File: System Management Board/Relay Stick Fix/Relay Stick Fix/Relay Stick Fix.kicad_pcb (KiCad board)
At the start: 4 copper layers, 28.2 x 27 mm, 17 parts, among them J1 Conn_02x06, Q1 NMOS, U2 74LVC1G04

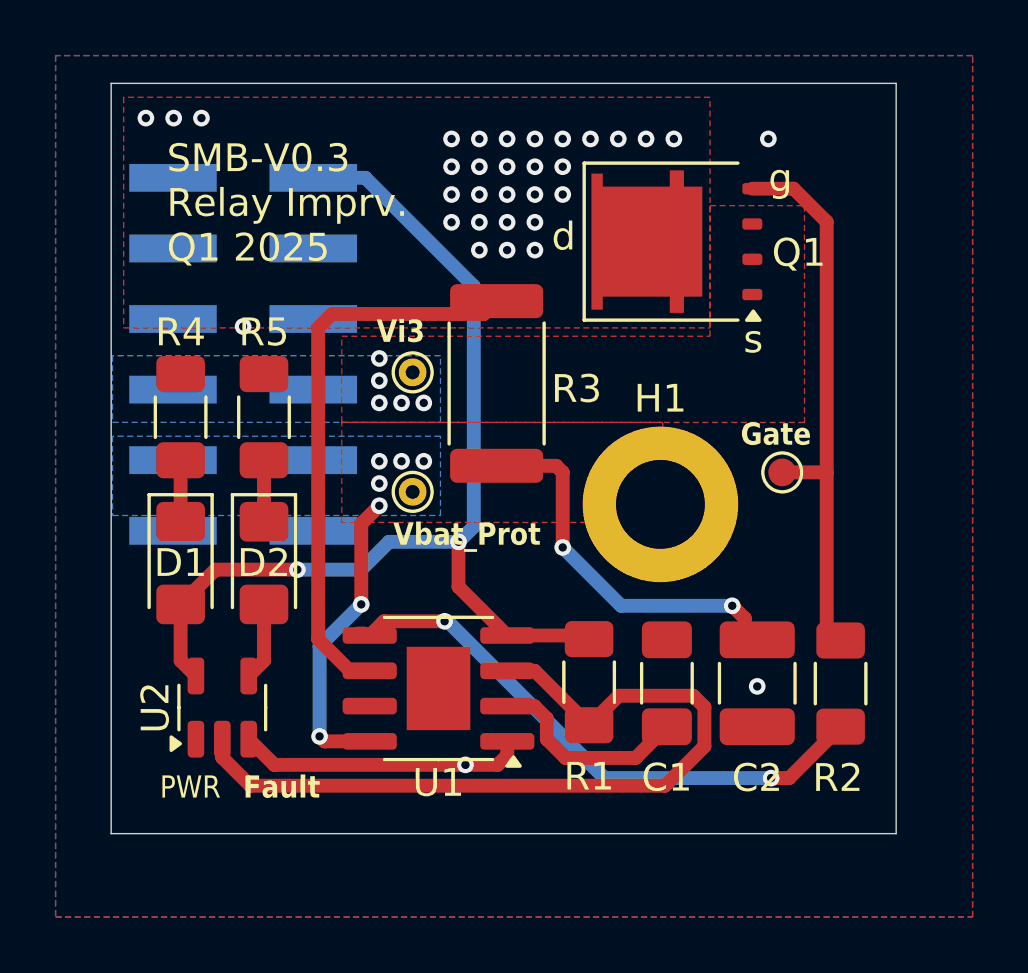
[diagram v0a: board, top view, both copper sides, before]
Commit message: fixed a mjor issue where 5V boot strap and GND headers were reversed
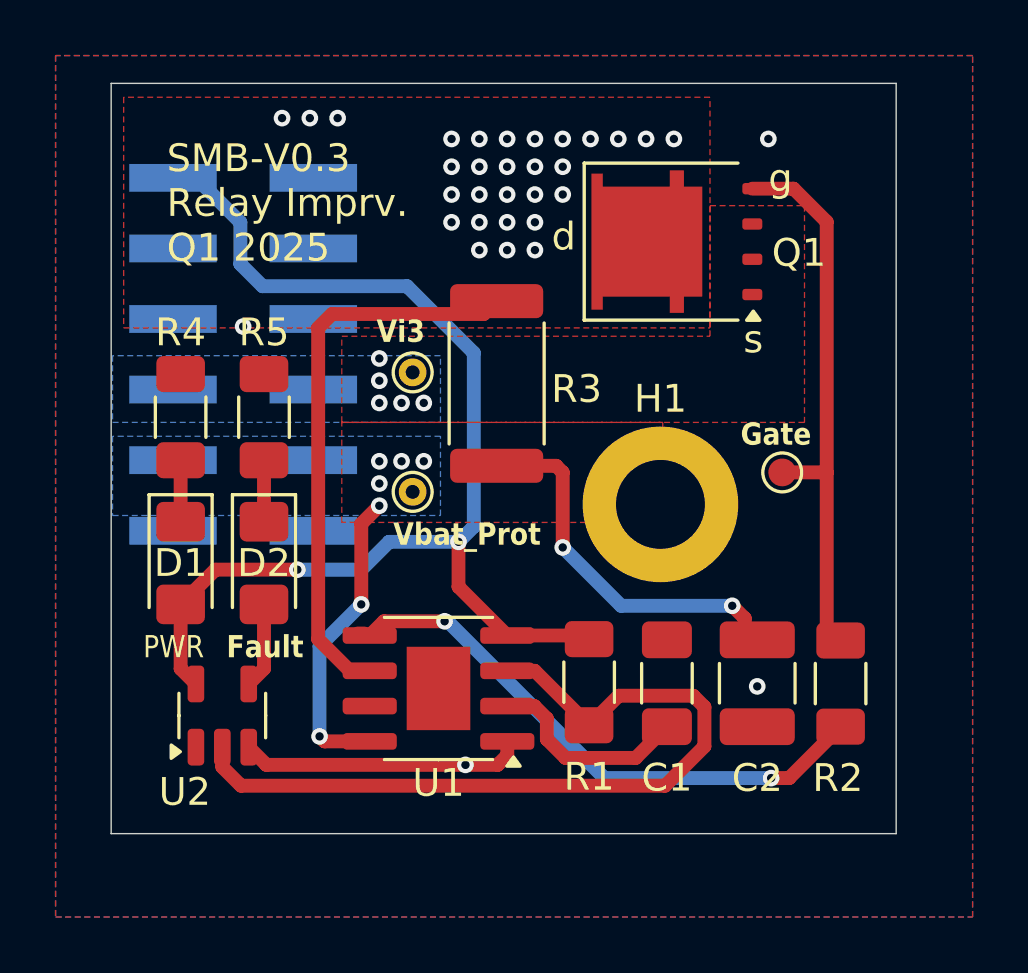
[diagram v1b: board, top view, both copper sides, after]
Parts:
- R3: value 0 -> .001
- moved U2 0.29 mm to (19.9, 37.8)
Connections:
- J1 pad 1: /5V Bootstrap -> GND
- J1 pad 2: GND -> /5V Bootstrap
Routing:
- net /5V Bootstrap: track 38.3 -> 42.8 mm
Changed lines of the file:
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@@
 	(footprint "Package_TO_SOT_SMD:SOT-23-5"
 		(layer "F.Cu")
-		(at 19.85 37.4625 90)
+		(at 19.85 37.75 90)
 		(descr "SOT, 5 Pin (https://www.jedec.org/sites/default/files/docs/Mo-178c.PDF variant AA), generated with kicad-footprint-generator ipc_gullwing_generator.py")
 		(tags "SOT TO_SOT_SMD")
 		(property "Reference" "U2"
-			(at 0 -2.4 -90)
+			(at -2.75 -1.35 0)
 			(layer "F.SilkS")
 			(effects
@@
 			)
 		)
-		(property "Value" "0"
+		(property "Value" ".001"
 			(at 0 2.62 -90)
 			(layer "F.Fab")
@@
 			(size 3.15 1)
 			(layers "B.Cu" "B.Paste" "B.Mask")
-			(net 2 "/5V Bootstrap")
+			(net 1 "GND")
 			(pinfunction "Pin_1")
 			(pintype "passive")
@@
 			(size 3.15 1)
 			(layers "B.Cu" "B.Paste" "B.Mask")
-			(net 1 "GND")
+			(net 2 "/5V Bootstrap")
 			(pinfunction "Pin_2")
 			(pintype "passive")
@@
 	)
 	(gr_text "Fault"
-		(at 20.6 40.8 0)
+		(at 20 35.75 0)
 		(layer "F.SilkS")
 		(effects
@@
 	)
 	(gr_text "PWR\n"
-		(at 17.6 40.8 0)
+		(at 17 35.75 0)
 		(layer "F.SilkS")
 		(effects
@@
 	)
 	(segment
-		(start 28.6 39.525)
-		(end 29.76 39.525)
+		(start 20.8 38.8875)
+		(end 21.4375 39.525)
 		(width 0.5)
 		(layer "F.Cu")
@@
 	)
 	(segment
-		(start 20.8 38.6)
-		(end 21.725 39.525)
+		(start 28.6 39.525)
+		(end 29.76 39.525)
 		(width 0.5)
 		(layer "F.Cu")
@@
 	)
 	(segment
-		(start 21.725 39.525)
-		(end 28.6 39.525)
+		(start 30.105 39.18)
+		(end 30.105 38.68)
 		(width 0.5)
 		(layer "F.Cu")
@@
 	)
 	(segment
-		(start 30.105 39.18)
-		(end 30.105 38.68)
+		(start 21.4375 39.525)
+		(end 28.6 39.525)
 		(width 0.5)
 		(layer "F.Cu")
@@
 	)
 	(via
-		(at 17.1 16.25)
+		(at 22 16.25)
 		(size 0.6)
 		(drill 0.3)
@@
 	)
 	(via
-		(at 19.1 16.25)
+		(at 24 16.25)
 		(size 0.6)
 		(drill 0.3)
@@
 	)
 	(via
-		(at 18.1 16.25)
+		(at 23 16.25)
 		(size 0.6)
 		(drill 0.3)
@@
 	)
 	(segment
+		(start 23.125 18.4)
+		(end 23.325 18.2)
+		(width 0.2)
+		(layer "B.Cu")
+		(net 1)
+	)
+	(segment
 		(start 28.35 33.115)
 		(end 30.105 34.87)
@@
 	)
 	(segment
-		(start 18.35 35.775)
-		(end 18.9 36.325)
+		(start 18.35 33.75)
+		(end 18.35 36.0625)
 		(width 0.5)
 		(layer "F.Cu")
@@
 	)
 	(segment
-		(start 18.35 33.75)
-		(end 18.35 35.775)
+		(start 30.105 34.87)
+		(end 32.92 34.87)
 		(width 0.5)
 		(layer "F.Cu")
@@
 	)
 	(segment
-		(start 30.105 34.87)
-		(end 32.92 34.87)
+		(start 18.35 36.0625)
+		(end 18.9 36.6125)
 		(width 0.5)
 		(layer "F.Cu")
@@
 	)
 	(segment
+		(start 20.5 20)
+		(end 18.9 18.4)
+		(width 0.5)
+		(layer "B.Cu")
+		(net 2)
+	)
+	(segment
+		(start 28.9 30.95)
+		(end 28.9 24.7)
+		(width 0.5)
+		(layer "B.Cu")
+		(net 2)
+	)
+	(segment
 		(start 24.85 32.5)
 		(end 22.55 32.5)
@@
 	)
 	(segment
-		(start 28.35 31.5)
-		(end 28.9 30.95)
+		(start 21.3 22.3)
+		(end 20.5 21.5)
 		(width 0.5)
 		(layer "B.Cu")
@@
 	)
 	(segment
-		(start 25 18.4)
-		(end 23.125 18.4)
+		(start 20.5 21.5)
+		(end 20.5 20)
 		(width 0.5)
 		(layer "B.Cu")
@@
 	)
 	(segment
-		(start 28.9 30.95)
-		(end 28.9 22.3)
+		(start 28.35 31.5)
+		(end 28.9 30.95)
 		(width 0.5)
 		(layer "B.Cu")
@@
 	)
 	(segment
-		(start 28.9 22.3)
-		(end 25 18.4)
+		(start 26.5 22.3)
+		(end 21.3 22.3)
 		(width 0.5)
 		(layer "B.Cu")
@@
 	)
 	(segment
-		(start 25.85 31.5)
-		(end 24.85 32.5)
+		(start 28.9 24.7)
+		(end 26.5 22.3)
 		(width 0.5)
 		(layer "B.Cu")
@@
 	)
 	(segment
-		(start 23.125 18.4)
-		(end 23.325 18.2)
-		(width 0.2)
+		(start 18.9 18.4)
+		(end 18.075 18.4)
+		(width 0.5)
+		(layer "B.Cu")
+		(net 2)
+	)
+	(segment
+		(start 25.85 31.5)
+		(end 24.85 32.5)
+		(width 0.5)
 		(layer "B.Cu")
 		(net 2)
@@
 	)
 	(segment
-		(start 33.05 38.1)
-		(end 34.1125 37.0375)
+		(start 34.1125 37.0375)
+		(end 36.796878 37.0375)
 		(width 0.5)
 		(layer "F.Cu")
@@
 	)
 	(segment
-		(start 20.862501 40.275)
-		(end 19.85 39.262499)
+		(start 37.2 37.440622)
+		(end 37.2 38.859378)
 		(width 0.5)
 		(layer "F.Cu")
@@
 	)
 	(segment
-		(start 34.1125 37.0375)
-		(end 36.796878 37.0375)
+		(start 36.796878 37.0375)
+		(end 37.2 37.440622)
 		(width 0.5)
 		(layer "F.Cu")
@@
 	)
 	(segment
-		(start 36.796878 37.0375)
-		(end 37.2 37.440622)
+		(start 19.85 39.6)
+		(end 19.85 38.6)
 		(width 0.5)
 		(layer "F.Cu")
@@
 	)
 	(segment
-		(start 19.85 39.262499)
-		(end 19.85 38.6)
+		(start 20.525 40.275)
+		(end 19.85 39.6)
 		(width 0.5)
 		(layer "F.Cu")
@@
 	)
 	(segment
-		(start 37.2 38.859378)
-		(end 35.784378 40.275)
+		(start 35.784378 40.275)
+		(end 20.525 40.275)
 		(width 0.5)
 		(layer "F.Cu")
@@
 	)
 	(segment
-		(start 35.784378 40.275)
-		(end 20.862501 40.275)
+		(start 33.05 38.1)
+		(end 34.1125 37.0375)
 		(width 0.5)
 		(layer "F.Cu")
@@
 	)
 	(segment
-		(start 37.2 37.440622)
-		(end 37.2 38.859378)
+		(start 37.2 38.859378)
+		(end 35.784378 40.275)
 		(width 0.5)
 		(layer "F.Cu")
@@
 	(segment
 		(start 21.35 33.75)
-		(end 21.35 35.775)
+		(end 21.35 36.0625)
 		(width 0.5)
 		(layer "F.Cu")
@@
 	)
 	(segment
-		(start 21.35 35.775)
-		(end 20.8 36.325)
+		(start 21.35 36.0625)
+		(end 20.8 36.6125)
 		(width 0.5)
 		(layer "F.Cu")
